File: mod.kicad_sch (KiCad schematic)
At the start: 5 parts, among them Q4 MMBF4391, SW2 SW_DPST, U6 TL074, U7 TL072, U8 LM13700

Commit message: Finish schematic for modulation
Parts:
- added C12, C14: 22n, symbol Device:C
- added C13: 4.7u, symbol Device:C
- added D10, D4, D8, D9: 1N4148, symbol Device:D_Filled
- added D11: LED, symbol Device:LED
- added D5: 1N1418, symbol Device:D_Filled
- added D6, D7: 5.1V, symbol Device:D_Zener_Filled
- added J10: LFO OUT, symbol Connector:Conn_01x02_Socket
- added J11: OUT, symbol Connector:Conn_01x02_Socket
- added J5: GATE IN, symbol Connector:Conn_01x02_Socket
- added J6: AR OUT, symbol Connector:Conn_01x02_Socket
- added J7: SQUARE OUT, symbol Connector:Conn_01x02_Socket
- added J8: TRI OUT, symbol Connector:Conn_01x02_Socket
- added J9: SINE OUT, symbol Connector:Conn_01x02_Socket
- added Q5: 2N3906, symbol Simulation_SPICE:PNP
- added Q6: 2N3904, symbol Simulation_SPICE:NPN
- added R25, R29, R58: 10k, symbol Device:R_US
- added R26, R50, R52: 200k, symbol Device:R_US
- added R27: 91k, symbol Device:R_US
- added R28: 30k, symbol Device:R_US
- added R30, R32: 1M, symbol Device:R_US
- added R31, R36, R38, R54, R55: 47k, symbol Device:R_US
- added R33, R51: 1k, symbol Device:R_US
- added R34: 39k, symbol Device:R_US
- added R35, R49, R59: 3k, symbol Device:R_US
- added R37: 220, symbol Device:R_US
- added R39, R43, R48, R57, R60: 100k, symbol Device:R_US
- added R40: 5.6k, symbol Device:R_US
- added R41: 4.7k, symbol Device:R_US
- added R42: 1.8k, symbol Device:R_US
- added R44: 56k, symbol Device:R_US
- added R45: 18k, symbol Device:R_US
- added R46: 4.k, symbol Device:R_US
- added R47: 15k, symbol Device:R_US
- added R53: R_US, symbol Device:R_US
- added R56: 7.5k, symbol Device:R_US
- added R61: 3.9k, symbol Device:R_US
- added RV1, RV2: 1M, symbol Device:R_Potentiometer_US
- added RV3, RV4, RV5, RV6: 100k, symbol Device:R_Potentiometer_US
- added SW1: SW_SP3T, symbol Switch:SW_SP3T
- SW2: value SW_DPST -> GATE/TRIG
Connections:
- net GND: now reaches U6.12 (+)
- net GND: now also U6.9 (-), U8.13 (-), U8.4 (-), C13.2, D11.1 (K), D5.2 (A), D7.2 (A), J11.1 (Pin_1), J5.1 (Pin_1), J6.1 (Pin_1), J7.1 (Pin_1), J8.1 (Pin_1), J9.1 (Pin_1), R28.1, R30.2, R31.1, R37.2, R41.1, R42.1, R45.1, R48.1, R51.1, R53.1, R58.1, RV4.3, RV5.3, RV6.3
- net at U6.13 (-): now also C14.1, R36.2
- net at U6.14: now also C14.2, J8.2 (Pin_2), R38.1, R43.1, R60.2, SW1.2
- net at U8.7: now also U8.5, R52.2, R53.2
- net at U8.8: now also R54.2, RV6.1
- net at Q4.2 (S): now also SW2.1, C12.1, R30.1
- net at Q4.3 (G): now also Q5.2 (B), R25.2, R26.2
- net at U7.1: now also U7.2 (-), R49.2, R50.1
- net at U7.3 (+): now also R48.2, SW1.3
- net -12V: now reaches U7.4 (V-)
- net -12V: now also U6.11 (V-), U8.6 (V-), Q5.1 (C), R26.1, R46.1, R54.1, R56.2
- net +12V: now reaches U7.8 (V+)
- net +12V: now also U6.4 (V+), U8.11 (V+), R32.2, R44.2, R61.1, RV4.1, RV5.1
- net at U8.1: now also R55.1, R56.1
- net at U8.3 (+): now also R50.2, R51.2
- net at SW2.2: now also SW2.4, U6.5 (+), C12.2, D5.1 (K), R27.1, R28.2
- net at SW2.3: now also R29.2
- net at U6.6 (-): now also R31.2, R32.1, R34.1
- net at U6.7: now also R27.2, R33.1
- net at U6.10 (+): now also R38.2, R39.1
- net at U6.8: now also R39.2, R40.1, RV3.3
- net at U8.12: now also U8.10, R45.2, R47.2
- net at U8.14 (+): now also R42.2, R43.2
- net at U8.16: now also R44.1
- net at U8.9: now also J9.2 (Pin_2), R46.2, SW1.1
- net at U6.1: now also U6.2 (-), D10.2 (A), R35.1, R55.2
- net at U6.3 (+): now also C13.1, RV1.2, RV1.3, RV2.2, RV2.3
- net at U7.5 (+): now also R57.2, R58.2
- net at U7.6 (-): now also U7.7, R59.1
- new net: R47.1, RV4.2
- new net: D10.1 (K), R34.2
- new net: R37.1, RV3.1
- new net: R36.1, RV3.2
- new net: D4.2 (A), J5.2 (Pin_2)
- new net: D6.2 (A), D8.1 (K), D9.2 (A), R33.2
- new net: D8.2 (A), RV2.1
- new net: D9.1 (K), RV1.1
- new net: Q6.2 (B), R60.1
- new net: J7.2 (Pin_2), R40.2, R41.2, SW1.4
- new net: Q6.1 (C), R61.2
- new net: D11.2 (A), Q6.3 (E)
- new net: R57.1, RV6.2
- new net: R52.1, RV5.2
- new net: J6.2 (Pin_2), R35.2
- new net: Q5.3 (E), R29.1
- new net: J10.2 (Pin_2), R49.1
- new net: J11.2 (Pin_2), R59.2
- new net: D6.1 (K), D7.1 (K)
- new net GATE: D4.1 (K), R25.1
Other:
- moved on the sheet: Q4, SW2, U6A, U6B, U6C, U6D, U7A, U7B, U7C, U8A, U8B, U8C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

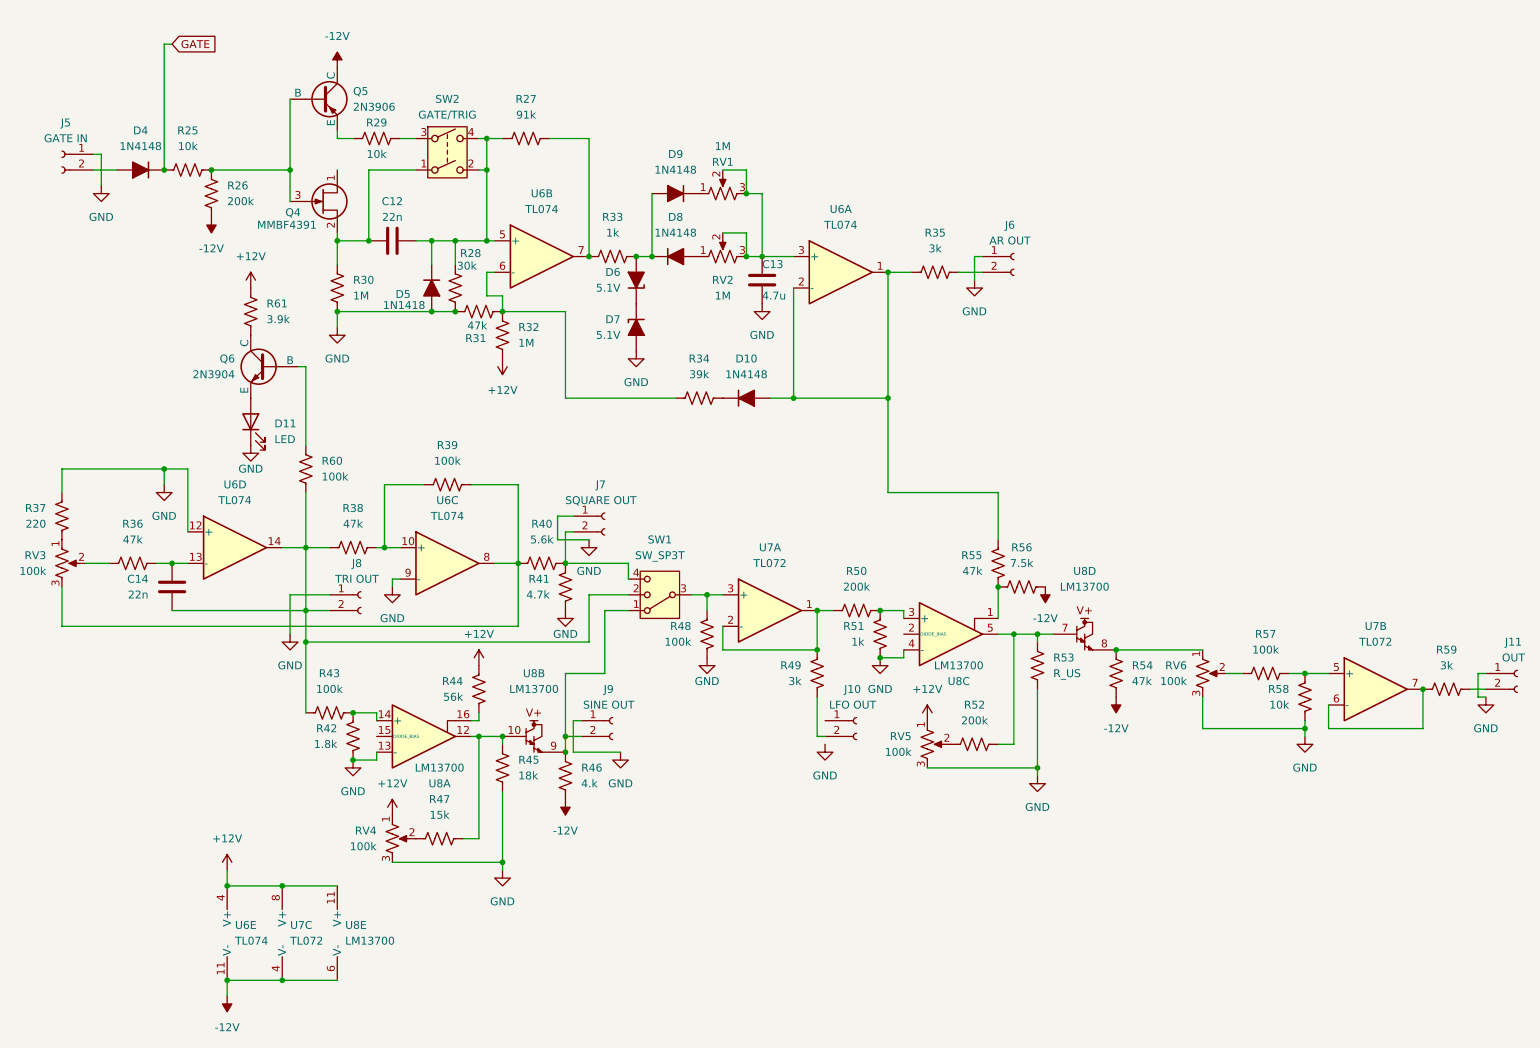
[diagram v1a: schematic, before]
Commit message: Schematic cleanup and placement
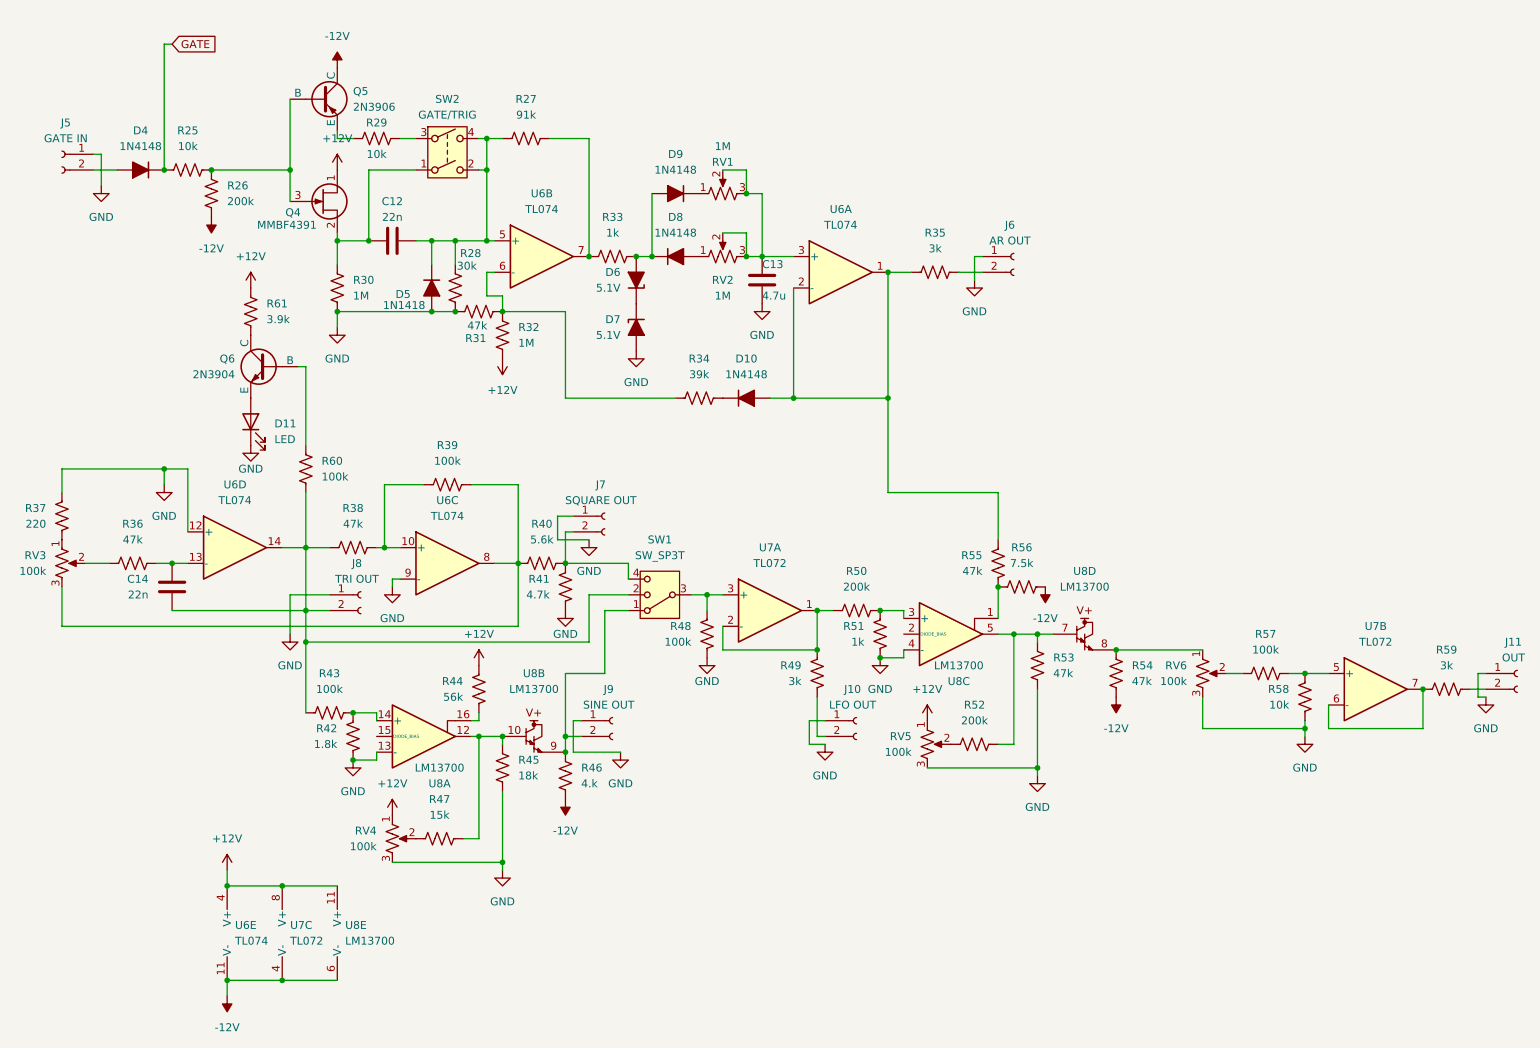
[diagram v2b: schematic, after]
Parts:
- C12, C14: footprint (none) -> Capacitor_THT:C_Disc_D3.0mm_W2.0mm_P2.50mm
- C13: footprint (none) -> Capacitor_THT:C_Radial_D6.3mm_H5.0mm_P2.50mm
- D10, D4, D5, D6, D7, D8, D9: footprint (none) -> Diode_THT:D_DO-35_SOD27_P7.62mm_Horizontal
- D11: footprint (none) -> LED_THT:LED_D3.0mm
- J10, J11, J5, J6, J7, J8, J9: footprint (none) -> Connector_Wire:SolderWire-0.75sqmm_1x02_P4.8mm_D1.25mm_OD2.3mm
- Q4: footprint Package_TO_SOT_SMD:SOT-23 -> Package_TO_SOT_THT:TO-92_Inline
- Q5, Q6: footprint (none) -> Package_TO_SOT_THT:TO-92_Inline
- R25, R26, R27, R28, R29, R30, R31, R32, R33, R34, R35, R36, R37, R38, R39, R40, R41, R42, R43, R44, R45, R46, R47, R48, R49, R50, R51, R52, R54, R55, R56, R57, R58, R59, R60, R61: footprint (none) -> Resistor_THT:R_Axial_DIN0207_L6.3mm_D2.5mm_P7.62mm_Horizontal
- R53: value R_US -> 47k; footprint (none) -> Resistor_THT:R_Axial_DIN0207_L6.3mm_D2.5mm_P7.62mm_Horizontal
- RV1, RV2, RV3, RV4, RV5, RV6: footprint (none) -> Connector_Wire:SolderWire-0.75sqmm_1x03_P4.8mm_D1.25mm_OD2.3mm
- SW1, SW2: footprint (none) -> Connector_Wire:SolderWire-0.75sqmm_1x04_P4.8mm_D1.25mm_OD2.3mm
- U6: footprint (none) -> Package_DIP:DIP-14_W7.62mm_Socket
- U7: footprint (none) -> Package_DIP:DIP-8_W7.62mm_Socket
- U8: footprint (none) -> Package_DIP:DIP-16_W7.62mm_Socket
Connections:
- net +12V: now also Q4.1 (D)
- net GND: now also J10.1 (Pin_1)
